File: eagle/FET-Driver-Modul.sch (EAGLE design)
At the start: 19 parts, among them X1 MKDSN1,5/3-5,08

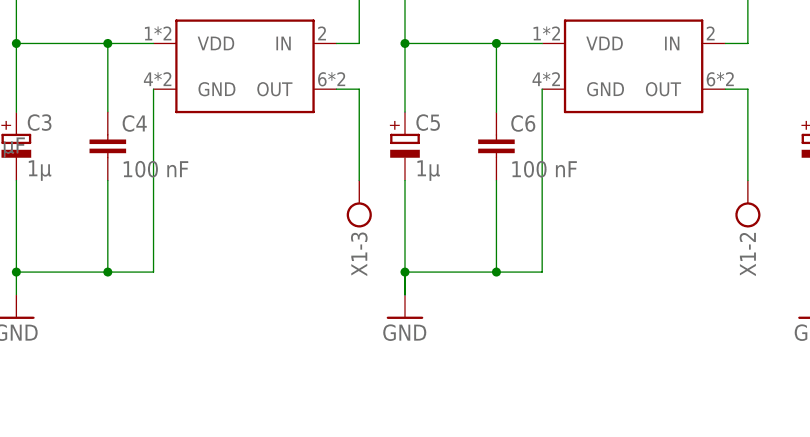
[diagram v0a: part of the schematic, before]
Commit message: added diode to driver power supply
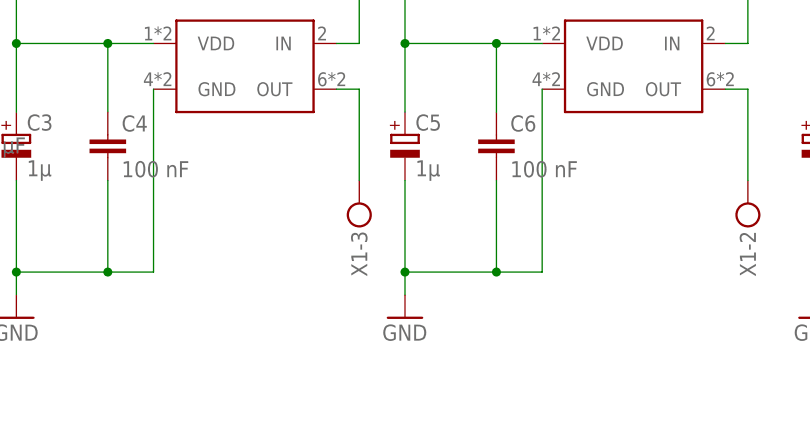
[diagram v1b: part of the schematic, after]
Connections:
- removed net GND1: C5.-, C6.2, U$4.GND
- net GND: now also C5.-, C6.2, U$4.GND
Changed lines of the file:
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@@
-</segment>
-<segment>
-<pinref part="GND29" gate="1" pin="GND"/>
-<wire x1="60.96" y1="-20.32" x2="60.96" y2="-17.78" width="0.1524" layer="91"/>
 </segment>
 <segment>
@@
 <wire x1="10.16" y1="-25.4" x2="10.16" y2="-27.94" width="0.1524" layer="91"/>
 </segment>
+<segment>
+<wire x1="60.96" y1="-17.78" x2="71.12" y2="-17.78" width="0.1524" layer="91"/>
+<pinref part="C5" gate="G$1" pin="-"/>
+<wire x1="60.96" y1="-7.62" x2="60.96" y2="-17.78" width="0.1524" layer="91"/>
+<pinref part="C6" gate="G$1" pin="2"/>
+<wire x1="71.12" y1="-7.62" x2="71.12" y2="-17.78" width="0.1524" layer="91"/>
+<pinref part="U$4" gate="G$1" pin="GND"/>
+<wire x1="76.2" y1="2.54" x2="76.2" y2="-17.78" width="0.1524" layer="91"/>
+<wire x1="76.2" y1="-17.78" x2="71.12" y2="-17.78" width="0.1524" layer="91"/>
+<junction x="71.12" y="-17.78"/>
+<pinref part="GND29" gate="1" pin="GND"/>
+<wire x1="60.96" y1="-17.78" x2="60.96" y2="-20.32" width="0.1524" layer="91"/>
+<junction x="60.96" y="-17.78"/>
+</segment>
 </net>
 <net name="N$33" class="0">
@@
 </segment>
 </net>
-<net name="GND1" class="0">
-<segment>
-<wire x1="60.96" y1="-20.32" x2="60.96" y2="-17.78" width="0.1524" layer="91"/>
-<wire x1="60.96" y1="-17.78" x2="71.12" y2="-17.78" width="0.1524" layer="91"/>
-<pinref part="C5" gate="G$1" pin="-"/>
-<wire x1="60.96" y1="-7.62" x2="60.96" y2="-17.78" width="0.1524" layer="91"/>
-<junction x="60.96" y="-17.78"/>
-<pinref part="C6" gate="G$1" pin="2"/>
-<wire x1="71.12" y1="-7.62" x2="71.12" y2="-17.78" width="0.1524" layer="91"/>
-<pinref part="U$4" gate="G$1" pin="GND"/>
-<wire x1="76.2" y1="2.54" x2="76.2" y2="-17.78" width="0.1524" layer="91"/>
-<wire x1="76.2" y1="-17.78" x2="71.12" y2="-17.78" width="0.1524" layer="91"/>
-<junction x="71.12" y="-17.78"/>
-</segment>
-</net>
